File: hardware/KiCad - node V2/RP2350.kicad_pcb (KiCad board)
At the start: 4 copper layers, 145.2 x 84.4 mm, 83 parts, among them J3 USB_C_Receptacle_USB2.0_14P, SW1 BOOTSEL, U1 RP2350A, U2 THVD1450D, U3 ADXL355BEZ, U4 TPS2121RUXR, U5 USBLC6-2SC6, U6 TLV75733PDBV, U7 W25Q128JVS, U8 TPS7A20xxxDBV

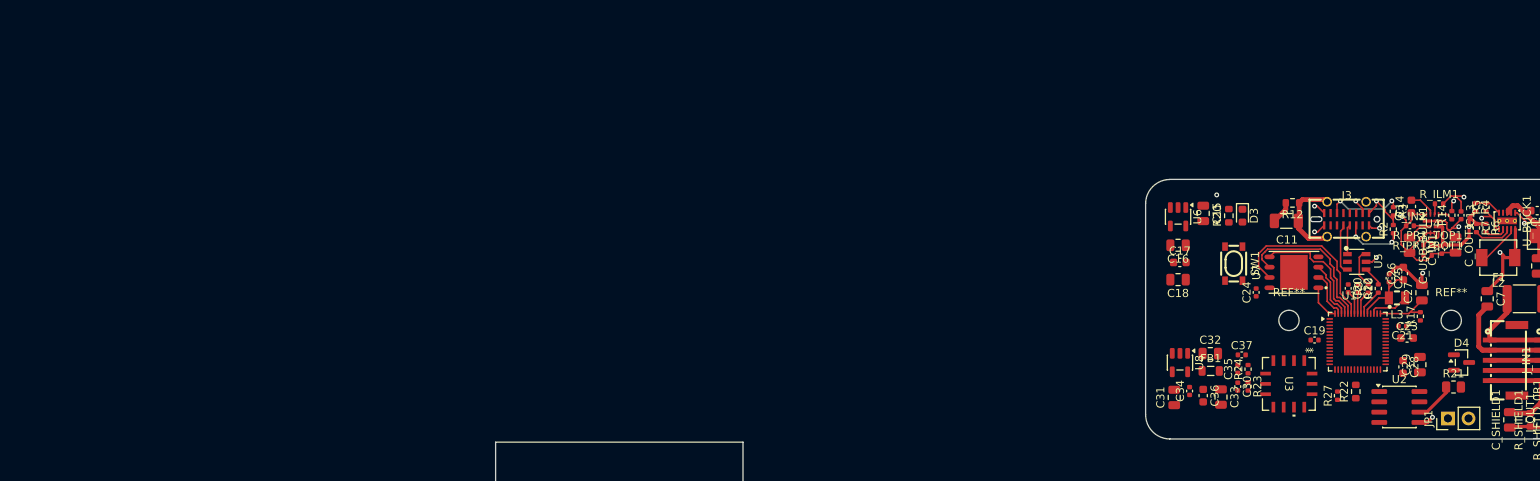
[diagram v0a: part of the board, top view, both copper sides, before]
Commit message: hardware: layout updates
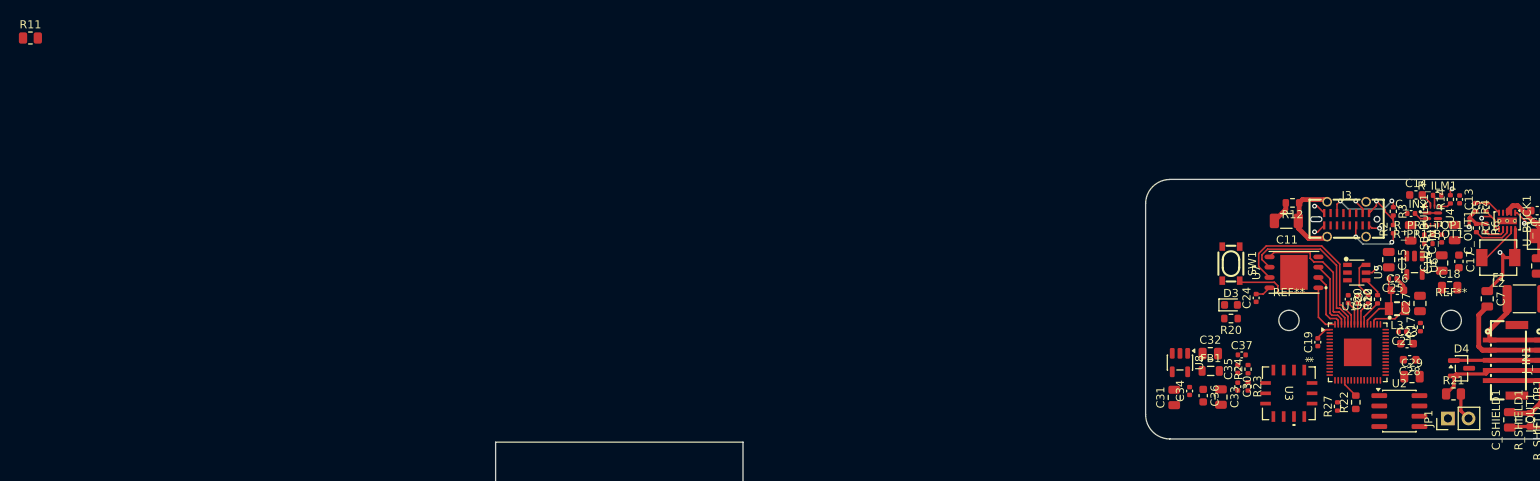
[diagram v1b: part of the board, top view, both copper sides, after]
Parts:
- added R11: 0 DNP, Resistor_SMD:R_0805_2012Metric, F.Cu at (1.71, 0.97)
- U4: footprint my_footprints:RUX0012A -> footprints:TPS2121RUXR-VQFN-HR-12_L2.5-W2.0-P0.50-BL
- moved C17 34.4 mm to (177.8, 28.5), turned to -90 degrees
- moved C18 33.5 mm to (176.7, 31.8), turned to 0 degrees
- moved C16 32.6 mm to (175.7, 28.7), turned to 90 degrees
- moved U6 29.8 mm to (172.3, 29.0)
- moved C15 23.6 mm to (169.2, 28.3)
- moved R20 12.7 mm to (149.7, 35.6), turned to 180 degrees
- moved D3 11.1 mm to (149.7, 33.9), turned to 0 degrees
- moved C26 2.18 mm to (170.2, 32.1), turned to 0 degrees
- moved C13 1.97 mm to (177.9, 20.9)
- moved R14 1.97 mm to (176.8, 20.9)
- moved C29 1.78 mm to (172.0, 42.7), turned to 0 degrees
- moved C14 1.53 mm to (172.5, 20.3), turned to 0 degrees
- moved C_IN2 1.53 mm to (171.9, 22.6)
- moved C_USB_BULK1 1.53 mm to (171.9, 25.0)
- moved C_OUT1 1.52 mm to (177.3, 25.0)
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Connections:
- R22 pad 2: Net-(U1-GPIO18) -> Net-(U1-GPIO15)
- U1 pad 19: unconnected-(U1-GPIO15-Pad19) -> Net-(U1-GPIO15)
- U1 pad 29: Net-(U1-GPIO18) -> unconnected-(U1-GPIO18-Pad29)
- U2 pad 2: Net-(U1-GPIO18) -> Net-(U1-GPIO15)
- U2 pad 3: Net-(U1-GPIO18) -> Net-(U1-GPIO15)
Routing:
- net /5V_SYS: track 39.6 -> 1.35 mm, vias 2 -> 0
- net GND: track 91.0 -> 59.0 mm, vias 13 -> 9
- net Net-(U1-~{QSPI_SS}): track 4.44 -> 16.8 mm
- net /USB_VBUS: track 15.7 -> 5.06 mm
- net /5V_BUCK: track 29.9 -> 20.6 mm
- net Net-(U1-VREG_AVDD): track 7.01 -> 0.00 mm
- net /USB DN: track 6.20 -> 0.00 mm
- net /RS485_B: track 6.35 -> 10.8 mm
- net Net-(U4-PR1): track 4.03 -> 0.00 mm
- net /USB DP: track 3.66 -> 0.00 mm
- net /3V3_DIG: track 6.96 -> 10.4 mm
- net Net-(JP1-B): track 0.00 -> 3.41 mm
- net Net-(U1-GPIO15): track 0.00 -> 2.45 mm
- net /RS485_A: track 11.3 -> 13.7 mm
- net Net-(U1-QSPI_SD2): track 7.10 -> 8.65 mm
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
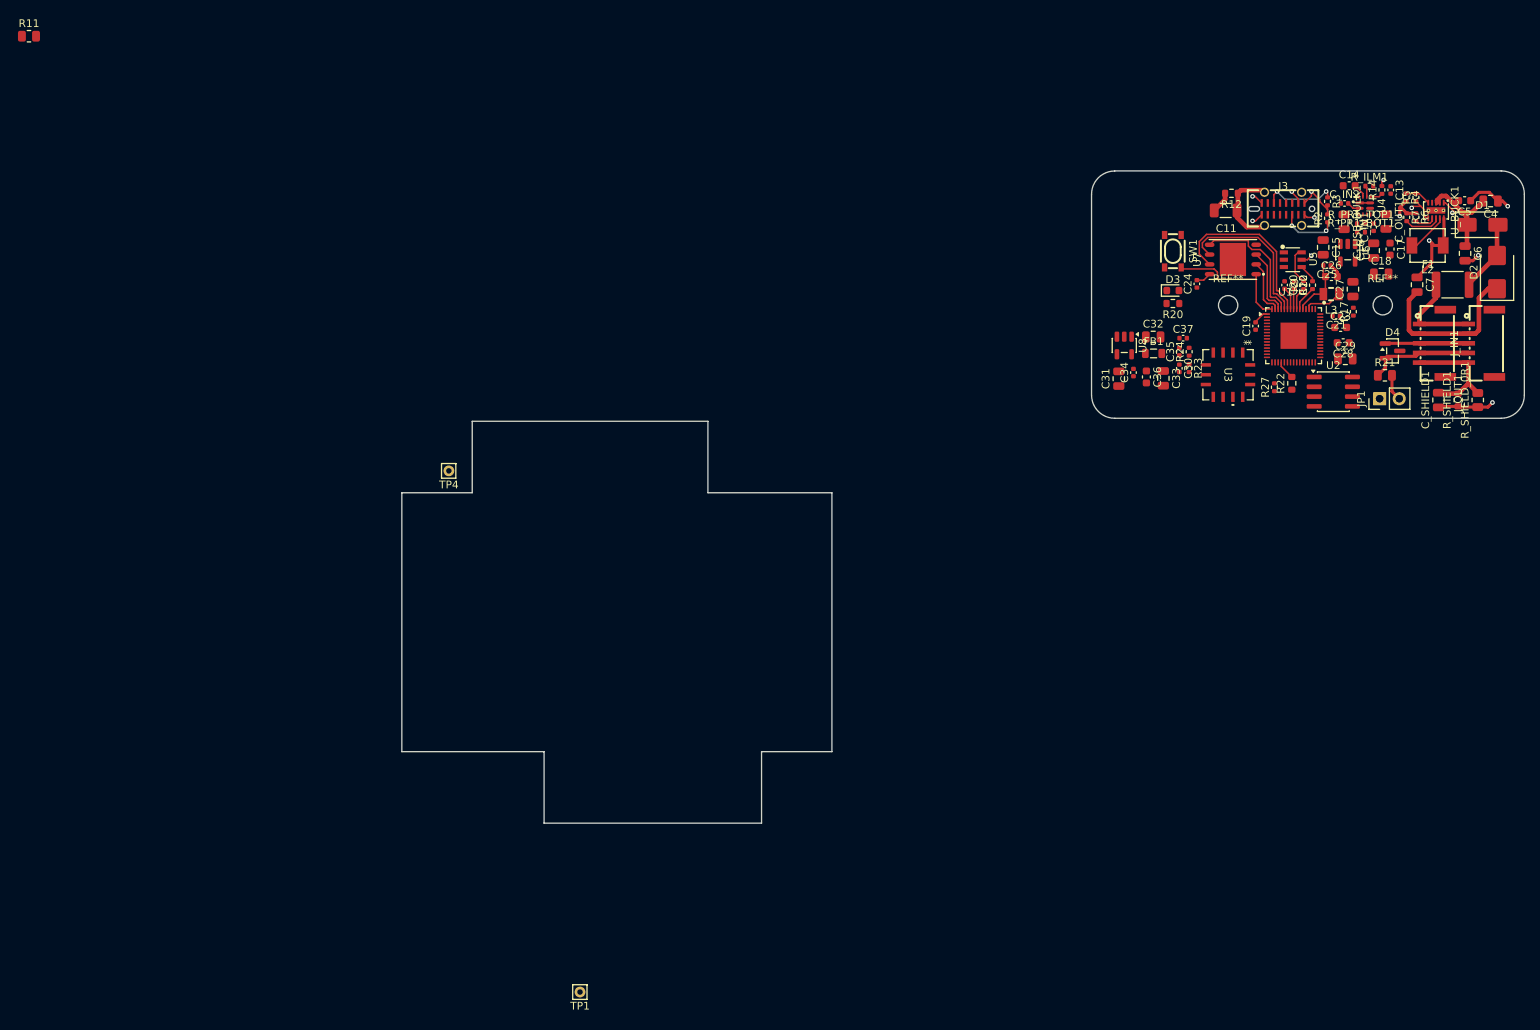
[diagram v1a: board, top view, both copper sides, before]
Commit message: hardware: layout updates
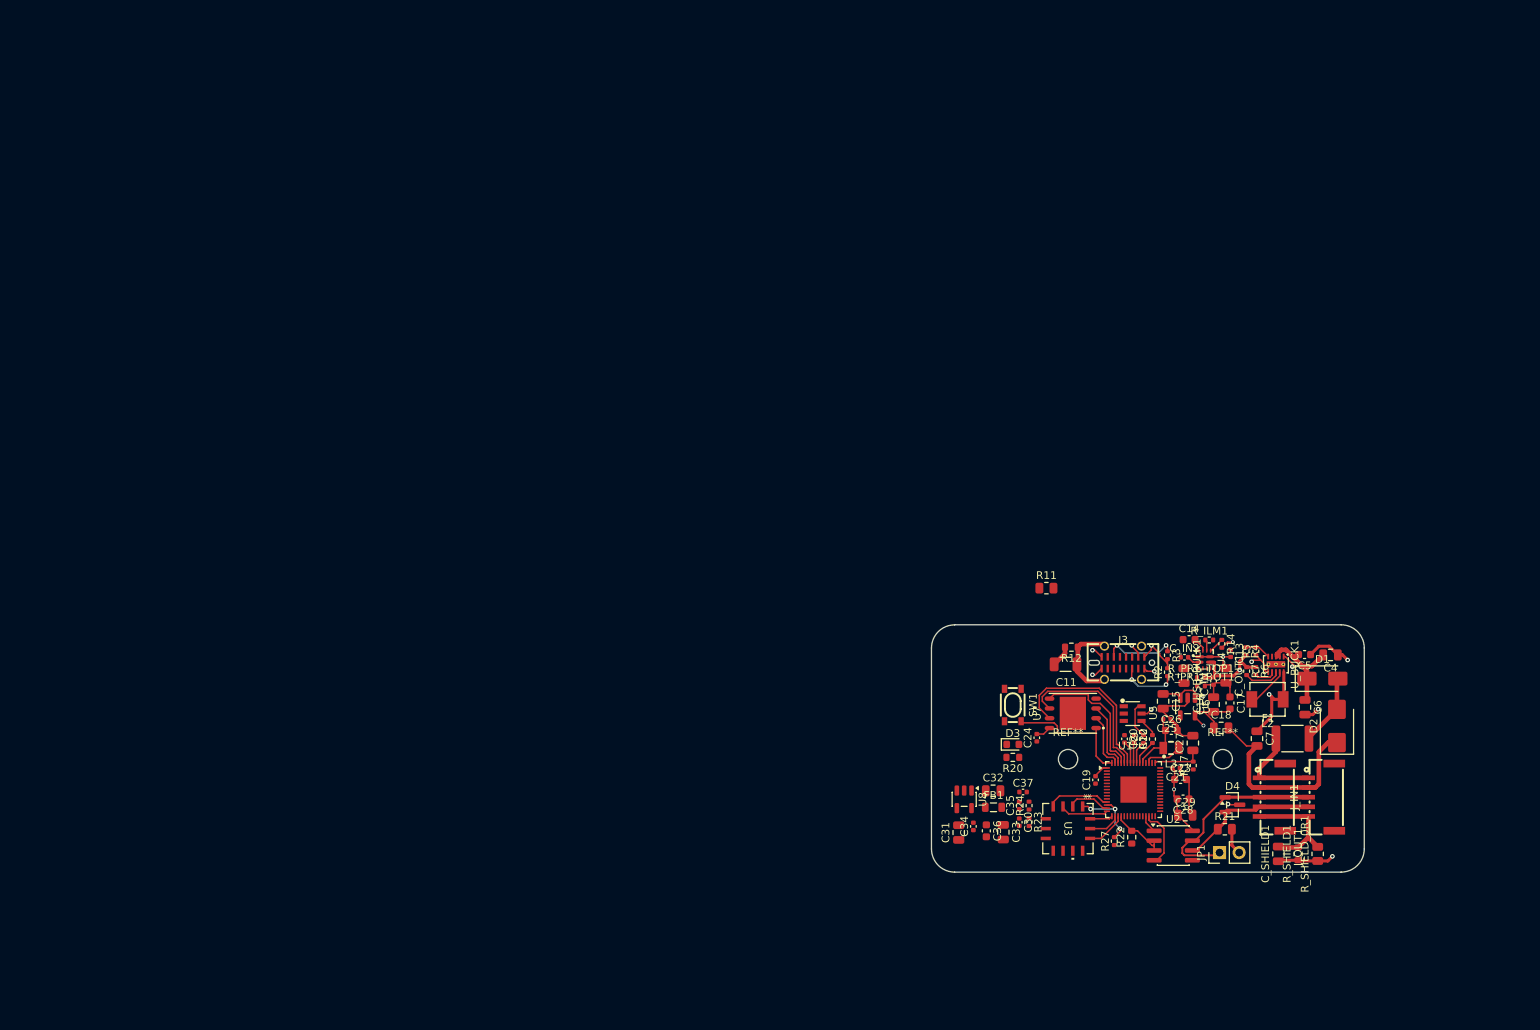
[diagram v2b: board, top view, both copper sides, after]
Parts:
- removed TP1: 5V_SYS, Connector_Pin:Pin_D0.7mm_L6.5mm_W1.8mm_FlatFork
- removed TP4: 12V_Protected, Connector_Pin:Pin_D0.7mm_L6.5mm_W1.8mm_FlatFork
- moved R11 149.8 mm to (133.3, 72.4)
- moved C13 63.4 mm to (157.2, 80.8)
- moved C28 62.6 mm to (151.0, 99.7)
- moved C29 62.6 mm to (151.3, 101.8)
- moved FB1 62.3 mm to (126.5, 100.7)
- moved U8 62.3 mm to (122.7, 99.7)
- moved C19 62.3 mm to (139.7, 97.2)
- moved C31 62.3 mm to (122.0, 104.0)
- moved C36 62.3 mm to (125.6, 103.8)
- moved C7 62.3 mm to (160.6, 91.9)
- moved F1 62.3 mm to (165.2, 91.9)
- moved R10 62.3 mm to (147.1, 91.9)
- moved R9 62.3 mm to (145.9, 91.9)
- moved U1 62.3 mm to (144.6, 98.5)
- moved U2 62.3 mm to (149.8, 105.7)
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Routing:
- net /3V3_DIG: track 10.4 -> 39.6 mm, vias 1 -> 3
- net GND: track 59.0 -> 86.7 mm, vias 9 -> 10
- net /5V_SYS: track 1.35 -> 18.7 mm, vias 0 -> 2
- net /RS485_B: track 10.8 -> 25.8 mm
- net /ADXL_CS: track 0.00 -> 9.83 mm, vias 0 -> 3
- net /ADXL_MISO: track 0.00 -> 8.15 mm
- net Net-(U1-GPIO17): track 0.00 -> 7.75 mm
- net /5V_BUCK: track 20.6 -> 28.1 mm
- net Net-(U1-VREG_AVDD): track 0.00 -> 6.48 mm
- net /ADXL_MOSI: track 0.00 -> 6.34 mm
- net /ADXL_SCLK: track 0.00 -> 5.54 mm
- net /ADXL_INT1: track 0.00 -> 5.20 mm
- net Net-(U1-GPIO15): track 2.45 -> 7.40 mm
- net /RS485_A: track 13.7 -> 18.1 mm
- net /ADXL_INT2: track 0.00 -> 4.18 mm
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- removed copper zone on In1.Cu, net GND
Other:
- board size 145.2 x 84.4 mm -> 56 x 32 mm

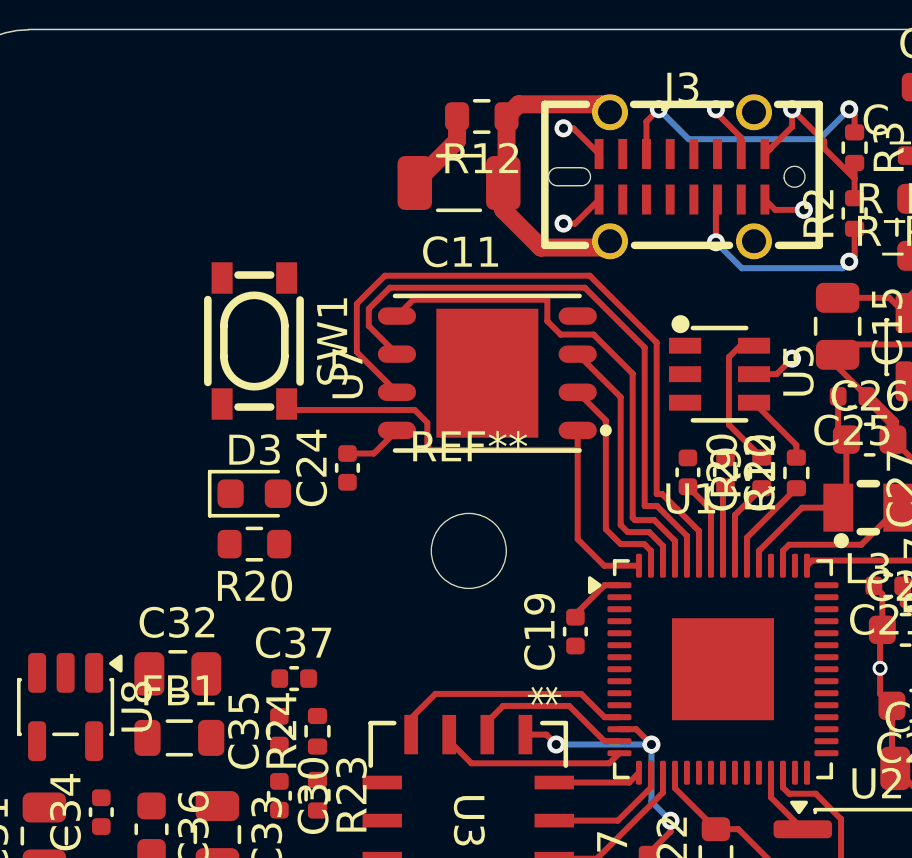
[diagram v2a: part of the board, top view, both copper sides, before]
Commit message: hardware: layout updates
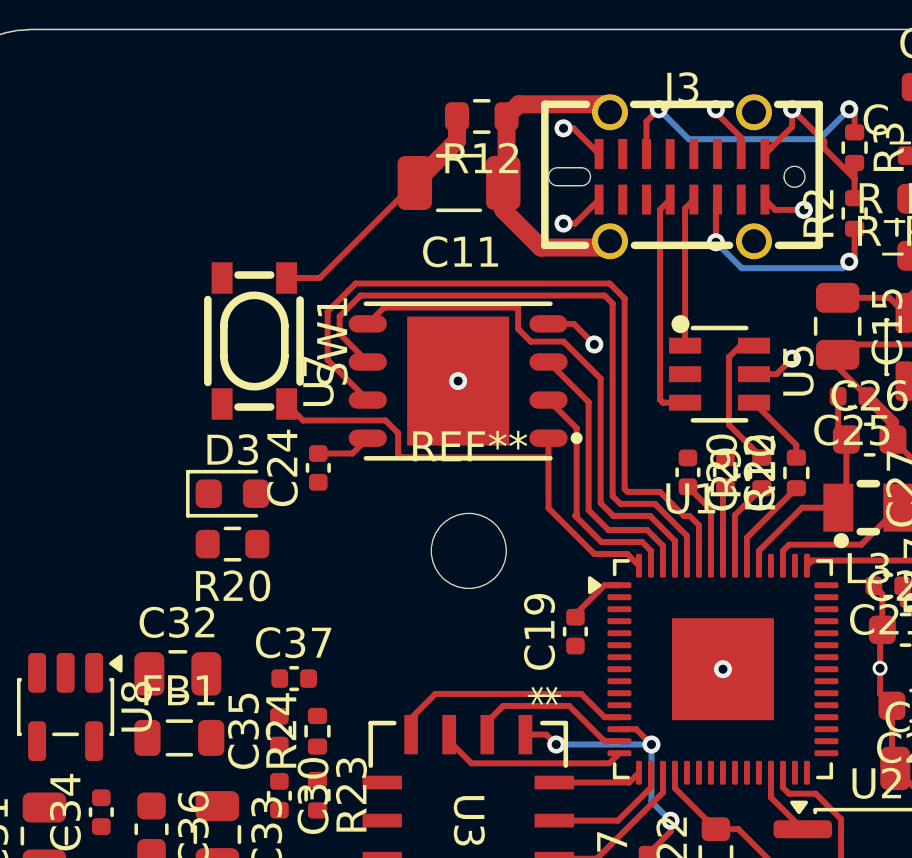
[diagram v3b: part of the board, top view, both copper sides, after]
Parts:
- moved U7 1.01 mm to (135.8, 88.8)
- moved C24 0.97 mm to (131.1, 91.7)
- moved R20 0.73 mm to (128.3, 94.3)
- moved D3 0.73 mm to (128.3, 92.6)
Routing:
- net /USB DN: track 0.00 -> 7.69 mm
- net GND: track 86.7 -> 94.1 mm, vias 10 -> 13
- net /USB DP: track 0.00 -> 4.99 mm
- net Net-(U1-QSPI_SD3): track 22.9 -> 24.7 mm
- net Net-(U1-QSPI_SCLK): track 20.3 -> 21.8 mm
- net Net-(U1-~{QSPI_SS}): track 16.8 -> 16.0 mm
- net Net-(U1-QSPI_SD1): track 7.25 -> 7.77 mm

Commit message: work in progress
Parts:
- moved R11 34.9 mm to (126.6, 38.1)
- moved C14 0.42 mm to (151.9, 79.5)
- moved C15 0.42 mm to (148.5, 87.4)
- moved C20 0.42 mm to (143.5, 92.3)
- moved C22 0.42 mm to (144.8, 92.3)
- moved C25 0.42 mm to (149.0, 89.8)
- moved C27 0.42 mm to (152.4, 92.8)
- moved C4 0.42 mm to (170.2, 81.4)
- moved C6 0.42 mm to (166.9, 88.2)
- moved C_IN2 0.42 mm to (151.3, 81.7)
- moved C_SHIELD1 0.42 mm to (163.5, 107.2)
- moved JP1 0.42 mm to (155.8, 107.0)
- moved L2 0.42 mm to (162.0, 87.2)
- moved R17 0.42 mm to (152.4, 95.8)
- moved R22 0.42 mm to (144.5, 105.0)
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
